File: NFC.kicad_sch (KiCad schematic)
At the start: 7 parts, among them U9 ST25DV04KC

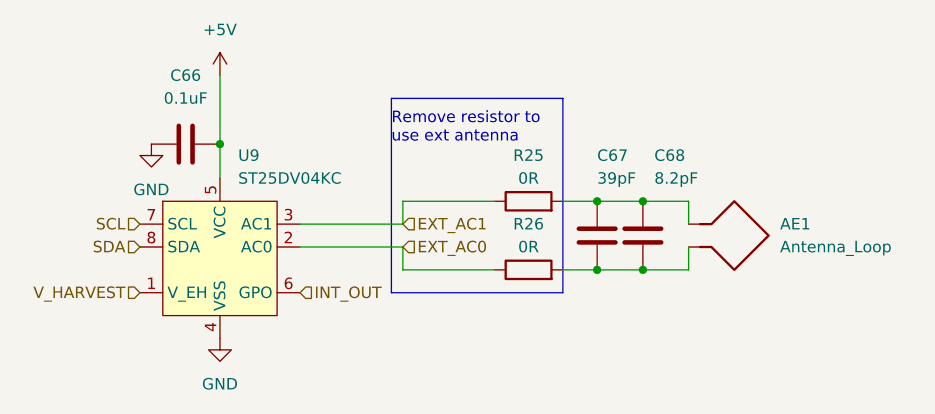
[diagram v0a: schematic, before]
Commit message: done first iteration of pcb routing, slikscreen still broken
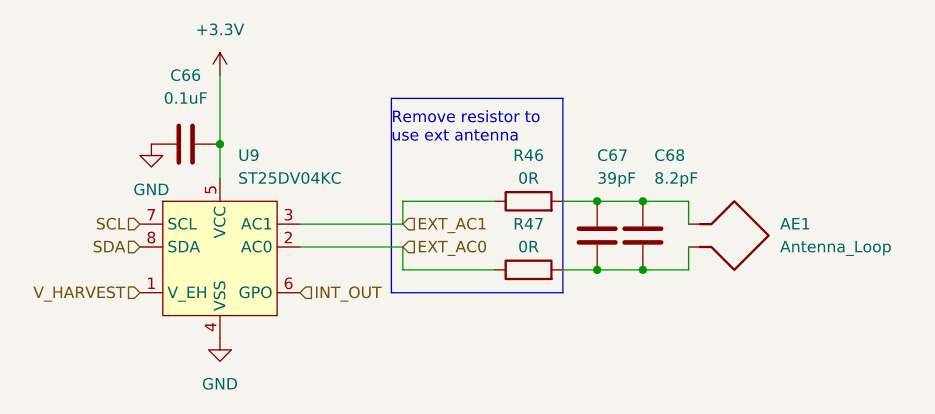
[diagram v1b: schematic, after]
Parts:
- renumbered R25 to R46, R26 to R47
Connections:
- net +5V renamed +3.3V
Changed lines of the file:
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@@
   (symbol (lib_id "power:GND") (at 133.35 69.85 0) (unit 1)
     (in_bom yes) (on_board yes) (fields_autoplaced)
-    (property "Reference" "#PWR078" (id 0) (at 133.35 76.2 0)
+    (property "Reference" "#PWR081" (id 0) (at 133.35 76.2 0)
       (effects (font (size 1.27 1.27)) hide)
     )
@@
   (symbol (lib_id "power:GND") (at 140.97 91.44 0) (unit 1)
     (in_bom yes) (on_board yes) (fields_autoplaced)
-    (property "Reference" "#PWR080" (id 0) (at 140.97 97.79 0)
+    (property "Reference" "#PWR083" (id 0) (at 140.97 97.79 0)
       (effects (font (size 1.27 1.27)) hide)
     )
@@
     (pin "2")
   )
+  (symbol (lib_id "power:+3.3V") (at 140.97 62.23 0) (unit 1)
+    (in_bom yes) (on_board yes) (fields_autoplaced)
+    (property "Reference" "#PWR?" (id 0) (at 140.97 66.04 0)
+      (effects (font (size 1.27 1.27)) hide)
+    )
+    (property "Value" "+3.3V" (id 1) (at 140.97 57.15 0))
+    (property "Footprint" "" (id 2) (at 140.97 62.23 0)
+      (effects (font (size 1.27 1.27)) hide)
+    )
+    (property "Datasheet" "" (id 3) (at 140.97 62.23 0)
+      (effects (font (size 1.27 1.27)) hide)
+    )
+    (pin "1")
+  )
   (symbol (lib_id "Device:C") (at 182.88 80.01 0) (unit 1)
     (in_bom yes) (on_board yes)
@@
     (pin "1")
     (pin "2")
-  )
-  (symbol (lib_id "power:+5V") (at 140.97 62.23 0) (unit 1)
-    (in_bom yes) (on_board yes) (fields_autoplaced)
-    (property "Reference" "#PWR079" (id 0) (at 140.97 66.04 0)
-      (effects (font (size 1.27 1.27)) hide)
-    )
-    (property "Value" "+5V" (id 1) (at 140.97 57.15 0))
-    (property "Footprint" "" (id 2) (at 140.97 62.23 0)
-      (effects (font (size 1.27 1.27)) hide)
-    )
-    (property "Datasheet" "" (id 3) (at 140.97 62.23 0)
-      (effects (font (size 1.27 1.27)) hide)
-    )
-    (pin "1")
   )
   (symbol (lib_id "airsoft_controller:ST25DV04KC") (at 140.97 82.55 0) (unit 1)
@@
   (symbol (lib_id "Device:R") (at 175.26 83.82 90) (unit 1)
     (in_bom yes) (on_board yes)
-    (property "Reference" "R26" (id 0) (at 175.26 78.74 90))
+    (property "Reference" "R47" (id 0) (at 175.26 78.74 90))
     (property "Value" "0R" (id 1) (at 175.26 81.28 90))
     (property "Footprint" "Resistor_SMD:R_0603_1608Metric_Pad0.98x0.95mm_HandSolder" (id 2) (at 175.26 85.598 90)
@@
   (symbol (lib_id "Device:R") (at 175.26 76.2 90) (unit 1)
     (in_bom yes) (on_board yes)
-    (property "Reference" "R25" (id 0) (at 175.26 71.12 90))
+    (property "Reference" "R46" (id 0) (at 175.26 71.12 90))
     (property "Value" "0R" (id 1) (at 175.26 73.66 90))
     (property "Footprint" "Resistor_SMD:R_0603_1608Metric_Pad0.98x0.95mm_HandSolder" (id 2) (at 175.26 77.978 90)

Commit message: mounting holes, fixes silkscreen
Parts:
- renumbered R46 to R45, R47 to R46
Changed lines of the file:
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@@
   (symbol (lib_id "power:+3.3V") (at 140.97 62.23 0) (unit 1)
     (in_bom yes) (on_board yes) (fields_autoplaced)
-    (property "Reference" "#PWR?" (id 0) (at 140.97 66.04 0)
+    (property "Reference" "#PWR082" (id 0) (at 140.97 66.04 0)
       (effects (font (size 1.27 1.27)) hide)
     )
@@
   (symbol (lib_id "Device:R") (at 175.26 83.82 90) (unit 1)
     (in_bom yes) (on_board yes)
-    (property "Reference" "R47" (id 0) (at 175.26 78.74 90))
+    (property "Reference" "R46" (id 0) (at 175.26 78.74 90))
     (property "Value" "0R" (id 1) (at 175.26 81.28 90))
     (property "Footprint" "Resistor_SMD:R_0603_1608Metric_Pad0.98x0.95mm_HandSolder" (id 2) (at 175.26 85.598 90)
@@
   (symbol (lib_id "Device:R") (at 175.26 76.2 90) (unit 1)
     (in_bom yes) (on_board yes)
-    (property "Reference" "R46" (id 0) (at 175.26 71.12 90))
+    (property "Reference" "R45" (id 0) (at 175.26 71.12 90))
     (property "Value" "0R" (id 1) (at 175.26 73.66 90))
     (property "Footprint" "Resistor_SMD:R_0603_1608Metric_Pad0.98x0.95mm_HandSolder" (id 2) (at 175.26 77.978 90)
